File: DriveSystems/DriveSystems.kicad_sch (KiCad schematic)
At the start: 30 parts, among them J1 Raspberry_Pi_4, J2 RJ45, M1 Motor_Servo, M2 Motor_Servo, SW1 SW_Rotary_1x2_MP, U1 RoboClaw Motor Controller, U2 5304 Gear Motor, U3 5VDC 5A UBC-C PSU, U4 24V 5V10A DCDC Stepdown, U5 RoboClaw VClamp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

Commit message: Update DriveSystems.kicad_sch
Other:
- note removed: "Pin 1 represents Output Pin 2 represents Input Pin 3 represents (-)L2 light terminal Pin 4 represents (+)L2 light terminal"
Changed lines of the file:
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@@
 		(comment 3 "Contributer: Jesus Espinoza")
-	)
-	(text "Pin 1 represents Output\nPin 2 represents Input\nPin 3 represents (-)L2 light terminal\nPin 4 represents (+)L2 light terminal"
-		(exclude_from_sim no)
-		(at 34.29 20.066 0)
-		(effects
-			(font
-				(size 1.27 1.27)
-			)
-		)
 	)
 	(text "16AWG Wire"

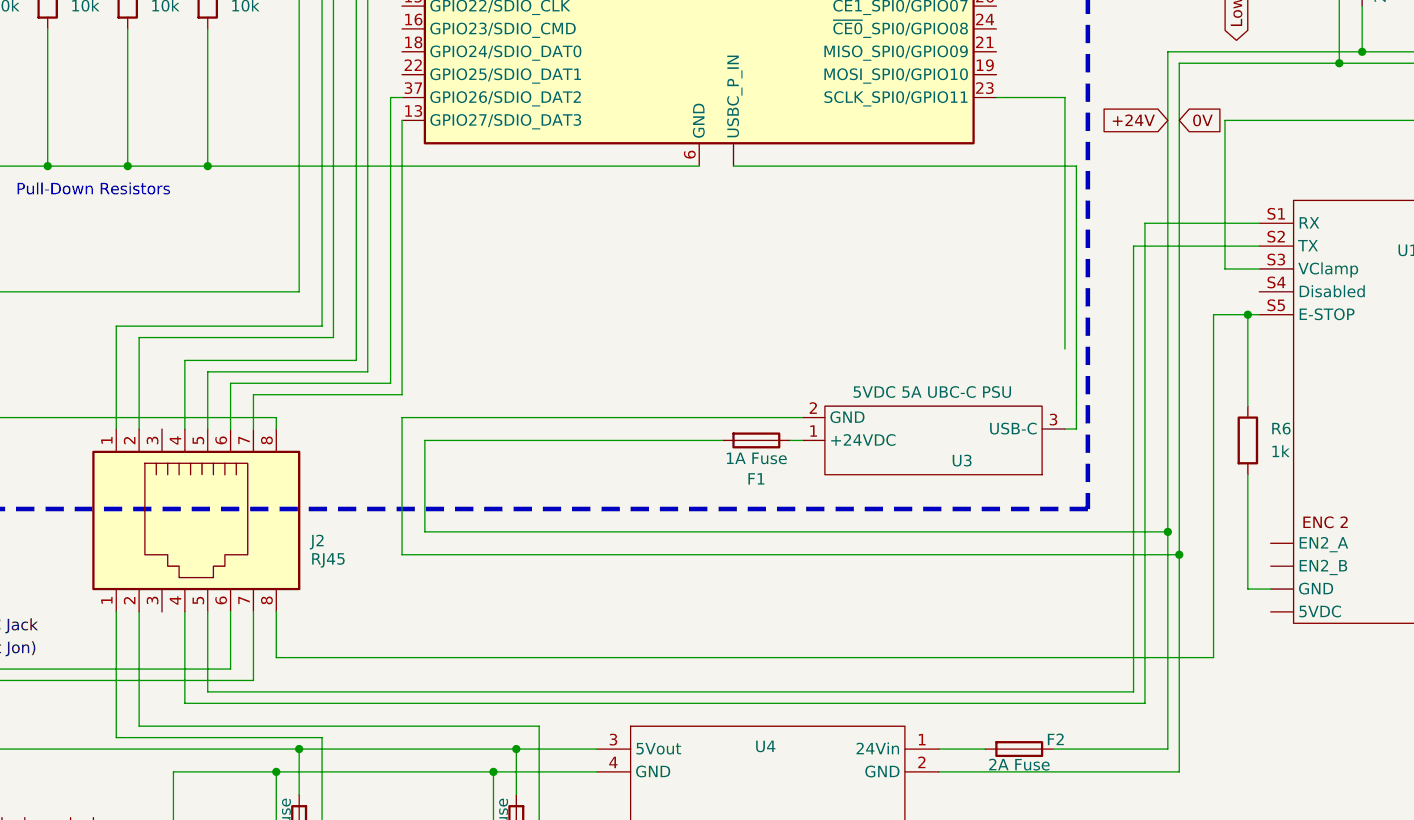
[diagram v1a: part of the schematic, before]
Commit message: Add ground connection
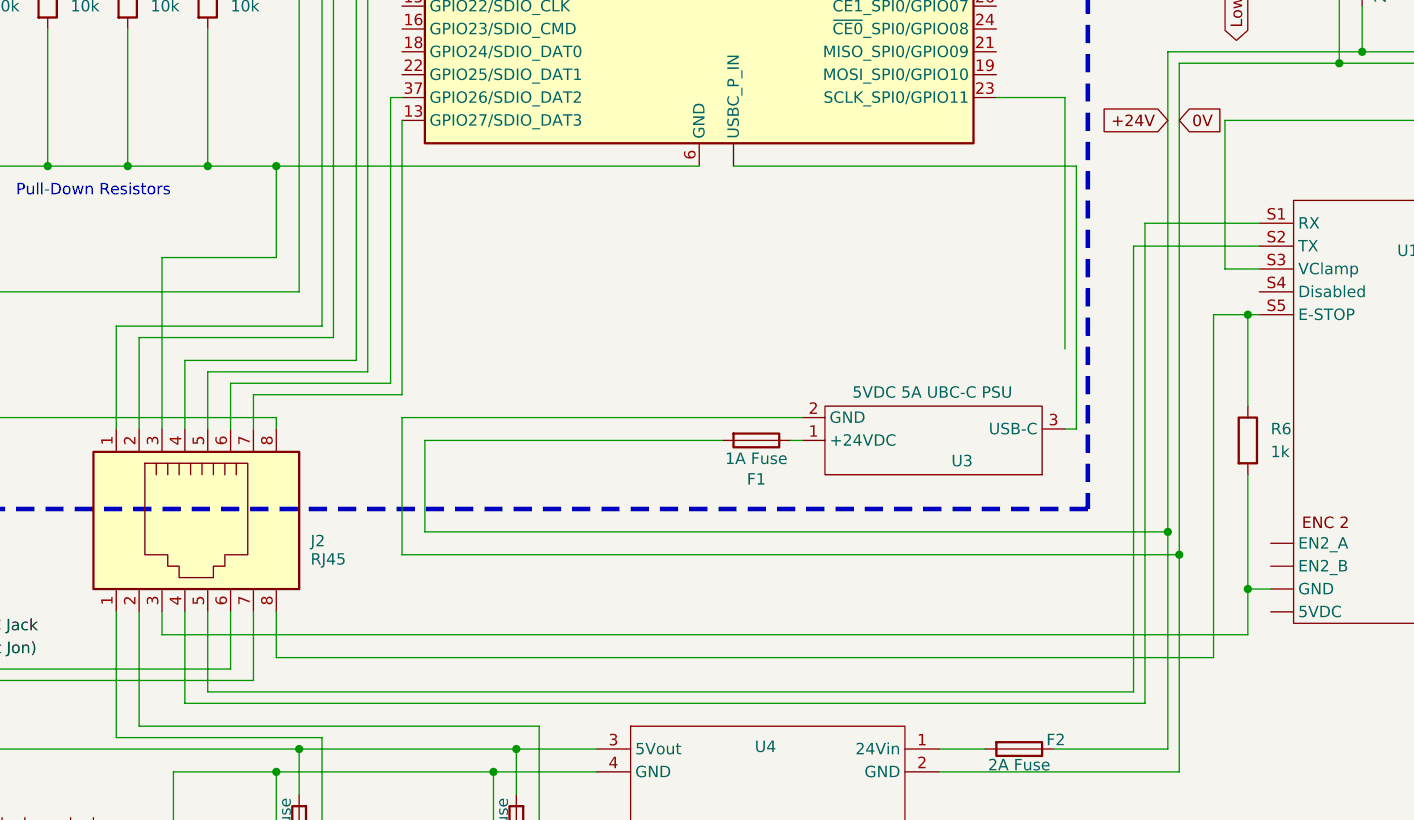
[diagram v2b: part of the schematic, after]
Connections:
- net at J1.14 (GND), J1.20 (GND), J1.25 (GND)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: now also J2.3
- net at R6.2, U1. (EN1_A): now also J2.3
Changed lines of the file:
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@@
+	)
+	(junction
+		(at 193.04 144.78)
+		(diameter 0)
+		(color 0 0 0 0)
 	)
 	(junction
@@
 	)
 	(junction
+		(at 85.09 97.79)
+		(diameter 0)
+		(color 0 0 0 0)
+	)
+	(junction
 		(at 205.74 85.09)
 		(diameter 0)
@@
 	(wire
 		(pts
-			(xy 77.47 97.79) (xy 132.08 97.79)
+			(xy 77.47 97.79) (xy 85.09 97.79)
 		)
 		(stroke
@@
 	(wire
 		(pts
+			(xy 72.39 107.95) (xy 72.39 127)
+		)
+		(stroke
+			(width 0)
+			(type default)
+			(color 240 149 36 1)
+		)
+	)
+	(wire
+		(pts
 			(xy 231.14 29.21) (xy 233.68 29.21)
 		)
@@
 	(wire
 		(pts
+			(xy 72.39 147.32) (xy 72.39 149.86)
+		)
+		(stroke
+			(width 0)
+			(type default)
+			(color 240 149 36 1)
+		)
+	)
+	(wire
+		(pts
 			(xy 109.22 176.53) (xy 109.22 165.1)
 		)
@@
 	(wire
 		(pts
+			(xy 193.04 149.86) (xy 193.04 144.78)
+		)
+		(stroke
+			(width 0)
+			(type default)
+			(color 240 149 36 1)
+		)
+	)
+	(wire
+		(pts
 			(xy 172.72 90.17) (xy 172.72 118.11)
 		)
@@
 			(width 0)
 			(type default)
+		)
+	)
+	(wire
+		(pts
+			(xy 85.09 97.79) (xy 85.09 107.95)
+		)
+		(stroke
+			(width 0)
+			(type default)
+			(color 240 149 36 1)
 		)
 	)
@@
 	(wire
 		(pts
+			(xy 72.39 149.86) (xy 193.04 149.86)
+		)
+		(stroke
+			(width 0)
+			(type default)
+			(color 240 149 36 1)
+		)
+	)
+	(wire
+		(pts
 			(xy 99.06 92.71) (xy 99.06 123.19)
 		)
@@
 	(wire
 		(pts
-			(xy 85.09 152.4) (xy 85.09 147.32)
+			(xy 85.09 147.32) (xy 85.09 152.4)
 		)
 		(stroke
@@
 	(wire
 		(pts
+			(xy 85.09 107.95) (xy 72.39 107.95)
+		)
+		(stroke
+			(width 0)
+			(type default)
+			(color 240 149 36 1)
+		)
+	)
+	(wire
+		(pts
 			(xy 226.06 144.78) (xy 241.3 144.78)
 		)
@@
 		)
 	)
+	(wire
+		(pts
+			(xy 85.09 97.79) (xy 132.08 97.79)
+		)
+		(stroke
+			(width 0)
+			(type default)
+			(color 240 149 36 1)
+		)
+	)

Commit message: As built
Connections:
- net at J1.10 (GPIO15/UART_RXD): now also J2.6; no longer J2.5
- net at J1.37 (GPIO26/SDIO_DAT2): now also J2.4; no longer J2.6
- net at J1.8 (GPIO14/UART_TXD): now also J2.5; no longer J2.4
- net at U1.S1 (RX): now also J2.5; no longer J2.4
- net at U1.S2 (TX): now also J2.6; no longer J2.5
- net at A1.9 (A0): now also J2.4; no longer J2.6

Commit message: Update DriveSystems.kicad_sch
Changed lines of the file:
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@@
 	(title_block
 		(title "REC 2025 ELECTRONIC SCHEMATIC")
-		(date "2025-04-01")
-		(rev "H")
+		(date "2025-04-06")
+		(rev "I")
 		(company "TERRIER RIDE ENGINEERING CLUB")
 		(comment 1 "Boston University")
@@
 	(wire
 		(pts
-			(xy 172.72 90.17) (xy 172.72 118.11)
-		)
-		(stroke
-			(width 0)
-			(type default)
-			(color 0 0 255 1)
-		)
-	)
-	(wire
-		(pts
 			(xy 241.3 161.29) (xy 246.38 161.29)
 		)
@@
 		)
 	)
-	(wire
-		(pts
-			(xy 172.72 90.17) (xy 165.1 90.17)
-		)
-		(stroke
-			(width 0)
-			(type default)
-			(color 0 0 255 1)
-		)
-	)
